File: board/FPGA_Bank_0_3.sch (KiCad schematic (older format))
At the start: 13 parts, among them U10 XC6SLX150T

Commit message: Issue #1680 - Bank 0 Ios
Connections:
- net MAC_SDA: now reaches U10.C1 (IO_L83P_3)
- net MAC_SCL: now reaches U10.G6 (*IO_L82N_3)
- net DIFFIO_B2N: now reaches U10.A17 (IO_L50N_0)
- net DIFFIO_A2N: now reaches U10.A5 (IO_L8N_VREF_0)
- net DIFFIO_B2P: now reaches U10.C17 (IO_L50P_0)
- net DIFFIO_A2P: now reaches U10.C5 (IO_L8P_0)
- net DIFFCLK_B0N: now reaches U10.E16 (IO_L37P_GCLK13_0)
- net DIFFCLK_A1P: now reaches U10.F10 (IO_L34N_GCLK18_0)
- net DIFFCLK_B1N: now reaches U10.F14 (IO_L36P_GCLK15_0)
- net DIFFCLK_B1P: now reaches U10.F15 (IO_L36N_GCLK14_0)
- net DIFFCLK_B0P: now reaches U10.F16 (IO_L37N_GCLK12_0)
- net DIFFIO_B3N: now reaches U10.F17 (IO_L51N_0)
- net DIFFIO_A3N: now reaches U10.F8 (IO_L7N_0)
- net DIFFIO_A1N: now reaches U10.F9 (IO_L32N_0)
- net DIFFCLK_A0P: now reaches U10.G11 (IO_L35N_GCLK16_0)
- net DIFFIO_B0N: now reaches U10.G13 (IO_L38N_VREF_0)
- net DIFFIO_B1N: now reaches U10.G15 (IO_L49N_0)
- net DIFFIO_B3P: now reaches U10.G16 (IO_L51P_0)
- net DIFFIO_A1P: now reaches U10.G8 (IO_L32P_0)
- net DIFFIO_A0P: now reaches U10.H10 (IO_L33P_0)
- net DIFFIO_A0N: now reaches U10.H11 (IO_L33N_0)
- net DIFFCLK_A0N: now reaches U10.H12 (IO_L35P_GCLK17_0)
- net DIFFIO_B0P: now reaches U10.H13 (IO_L38P_0)
- net DIFFIO_B1P: now reaches U10.H14 (IO_L49P_0)
- net RXAUXCH_N renamed DIFFIO_B4N
- net RXAUXCH_P renamed DIFFIO_B4P
- net RXCONFIG1 renamed DIFFIO_B5N
- net RXCONFIG2 renamed DIFFIO_B5P
- net RXHPD renamed DIFFIO_B6P
- net TXAUXCH_N renamed DIFFIO_YP
- net TXAUXCH_P renamed DIFFIO_YN
- net TXCONFIG1 renamed DIFFIO_ZP
- net TXCONFIG2 renamed DIFFIO_ZN
- net TXHPD renamed DIFFIO_B6N
- net USB_D0 renamed DIFFIO_A5P
- net USB_D1 renamed DIFFIO_A6N
- net USB_D2 renamed DIFFIO_A6P
- net USB_D3 renamed DIFFIO_XN
- net USB_D4 renamed DIFFIO_XP
- net USB_D5 renamed DIFFCLK_XN
- net USB_D6 renamed DIFFCLK_XP
- net USB_D7 renamed PCIE_RESET
- net USB_DIR renamed DIFFIO_A4N
- net USB_NXT renamed DIFFIO_A3P
- net USB_REFCLK renamed DIFFCLK_A1N
- net USB_RESETB renamed DIFFIO_A5N
- net USB_STP renamed DIFFIO_A4P
- no-connect marks 7 -> 31

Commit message: Issue #1683
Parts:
- U10: value XC6SLX150T -> XC6SLX45T
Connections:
- net DIFFCLK_A0N: now also U10.F15 (IO_L36N_GCLK14_0); no longer U10.H12 (IO_L35P_GCLK17_0)
- net DIFFCLK_A0P: now also U10.F14 (IO_L36P_GCLK15_0); no longer U10.G11 (IO_L35N_GCLK16_0)
- net DIFFCLK_B1N: now also U10.G11 (IO_L35N_GCLK16_0); no longer U10.F14 (IO_L36P_GCLK15_0)
- net DIFFCLK_B1P: now also U10.H12 (IO_L35P_GCLK17_0); no longer U10.F15 (IO_L36N_GCLK14_0)
- net DIFFCLK_XN: now also U10.D19 (IO_L62N_VREF_0); no longer U10.D5 (IO_L2N_0)
- net DIFFCLK_XP: now also U10.D18 (IO_L62P_0); no longer U10.D4 (IO_L2P_0)
- net DIFFIO_A0N: now also U10.C18 (IO_L66N_SCP0_0); no longer U10.H11 (IO_L33N_0)
- net DIFFIO_A0P: now also U10.D17 (IO_L66P_SCP1_0); no longer U10.H10 (IO_L33P_0)
- net DIFFIO_A1N: now also U10.A18 (IO_L63N_SCP6_0); no longer U10.F9 (IO_L32N_0)
- net DIFFIO_A1P: now also U10.B18 (IO_L63P_SCP7_0); no longer U10.G8 (IO_L32P_0)
- net DIFFIO_A2N: now also U10.G15 (IO_L49N_0); no longer U10.A5 (IO_L8N_VREF_0)
- net DIFFIO_A2P: now also U10.H14 (IO_L49P_0); no longer U10.C5 (IO_L8P_0)
- net DIFFIO_A3N: now also U10.G13 (IO_L38N_VREF_0); no longer U10.F8 (IO_L7N_0)
- net DIFFIO_A3P: now also U10.H13 (IO_L38P_0); no longer U10.F7 (IO_L7P_0)
- net DIFFIO_A4N: now also U10.E6 (IO_L4N_0); no longer U10.A4 (IO_L6N_0)
- net DIFFIO_A4P: now also U10.E5 (IO_L4P_0); no longer U10.C4 (IO_L6P_0)
- net DIFFIO_A5N: now also U10.A4 (IO_L6N_0); no longer U10.A3 (IO_L5N_0)
- net DIFFIO_A5P: now also U10.C4 (IO_L6P_0); no longer U10.B3 (IO_L5P_0)
- net DIFFIO_A6N: now also U10.A2 (IO_L3N_0); no longer U10.E6 (IO_L4N_0)
- net DIFFIO_A6P: now also U10.B2 (IO_L3P_0); no longer U10.E5 (IO_L4P_0)
- net DIFFIO_B0N: now also U10.A20 (IO_L65N_SCP2_0); no longer U10.G13 (IO_L38N_VREF_0)
- net DIFFIO_B0P: now also U10.B20 (IO_L65P_SCP3_0); no longer U10.H13 (IO_L38P_0)
- net DIFFIO_B1N: now also U10.F17 (IO_L51N_0); no longer U10.G15 (IO_L49N_0)
- net DIFFIO_B1P: now also U10.G16 (IO_L51P_0); no longer U10.H14 (IO_L49P_0)
- net DIFFIO_B3N: now also U10.H11 (IO_L33N_0); no longer U10.F17 (IO_L51N_0)
- net DIFFIO_B3P: now also U10.H10 (IO_L33P_0); no longer U10.G16 (IO_L51P_0)
- net DIFFIO_B4N: now also U10.D5 (IO_L2N_0); no longer U10.D19 (IO_L62N_VREF_0)
- net DIFFIO_B4P: now also U10.D4 (IO_L2P_0); no longer U10.D18 (IO_L62P_0)
- net DIFFIO_B5N: now also U10.A5 (IO_L8N_VREF_0); no longer U10.A18 (IO_L63N_SCP6_0)
- net DIFFIO_B5P: now also U10.C5 (IO_L8P_0); no longer U10.B18 (IO_L63P_SCP7_0)
- net DIFFIO_B6N: now also U10.A3 (IO_L5N_0); no longer U10.A19 (IO_L64N_SCP4_0)
- net DIFFIO_B6P: now also U10.B3 (IO_L5P_0); no longer U10.C19 (IO_L64P_SCP5_0)
- net DIFFIO_XN: now also U10.A19 (IO_L64N_SCP4_0); no longer U10.A2 (IO_L3N_0)
- net DIFFIO_XP: now also U10.C19 (IO_L64P_SCP5_0); no longer U10.B2 (IO_L3P_0)
- net DIFFIO_YN: now also U10.F8 (IO_L7N_0); no longer U10.B20 (IO_L65P_SCP3_0)
- net DIFFIO_YP: now also U10.F7 (IO_L7P_0); no longer U10.A20 (IO_L65N_SCP2_0)
- net DIFFIO_ZN: now also U10.F9 (IO_L32N_0); no longer U10.D17 (IO_L66P_SCP1_0)
- net DIFFIO_ZP: now also U10.G8 (IO_L32P_0); no longer U10.C18 (IO_L66N_SCP0_0)
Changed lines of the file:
@@
 $Descr A2 23386 16535
 encoding utf-8
-Sheet 11 12
+Sheet 12 12
 Title "HDMI2USB"
-Date "23 mar 2015"
+Date "25 mar 2015"
 Rev "Rev2"
 Comp ""
@@
 P 3300 6300
 F 0 "U10" H 2350 10350 60  0000 C CNN
-F 1 "XC6SLX150T" H 2650 -1000 60  0000 C CNN
+F 1 "XC6SLX45T" H 2650 -1000 60  0000 C CNN
 F 2 "~" H 3350 6300 60  0000 C CNN
 F 3 "~" H 3350 6300 60  0000 C CNN
@@
 P 19950 9550
 F 0 "U10" H 19000 13600 60  0000 C CNN
-F 1 "XC6SLX150T" H 19300 2250 60  0000 C CNN
+F 1 "XC6SLX45T" H 19300 2250 60  0000 C CNN
 F 2 "~" H 20000 9550 60  0000 C CNN
 F 3 "~" H 20000 9550 60  0000 C CNN
@@
 $EndComp
 $Comp
-L GND #PWR041
+L GND #PWR044
 U 1 1 52E58ED4
 P 12850 14050
-F 0 "#PWR041" H 12850 14050 30  0001 C CNN
+F 0 "#PWR044" H 12850 14050 30  0001 C CNN
 F 1 "GND" H 12850 13980 30  0001 C CNN
 F 2 "" H 12850 14050 60  0000 C CNN
@@
 	4100 1750 3650 1750
 $Comp
-L GND #PWR042
+L GND #PWR045
 U 1 1 52EB777D
 P 3650 1900
-F 0 "#PWR042" H 3650 1900 30  0001 C CNN
+F 0 "#PWR045" H 3650 1900 30  0001 C CNN
 F 1 "GND" H 3650 1830 30  0001 C CNN
 F 2 "" H 3650 1900 60  0000 C CNN
@@
 Connection ~ 9650 13150
 $Comp
-L GND #PWR043
+L GND #PWR046
 U 1 1 5387725D
 P 9850 13950
-F 0 "#PWR043" H 9850 13950 30  0001 C CNN
+F 0 "#PWR046" H 9850 13950 30  0001 C CNN
 F 1 "GND" H 9850 13880 30  0001 C CNN
 F 2 "" H 9850 13950 60  0000 C CNN
@@
 Text Notes 20050 2000 0    157  ~ 31
 BANK 0
-Text HLabel 19200 10150 0    39   BiDi ~ 0
+Text HLabel 19200 8750 0    39   BiDi ~ 0
 DIFFIO_B0P
-Text HLabel 19200 9950 0    39   BiDi ~ 0
+Text HLabel 19200 9550 0    39   BiDi ~ 0
 DIFFIO_B1P
 Text HLabel 19200 9750 0    39   BiDi ~ 0
 DIFFIO_B2P
-Text HLabel 19200 9550 0    39   BiDi ~ 0
+Text HLabel 19200 11150 0    39   BiDi ~ 0
 DIFFIO_B3P
-Text HLabel 19200 9350 0    39   BiDi ~ 0
+Text HLabel 19200 12750 0    39   BiDi ~ 0
 DIFFIO_B4P
-Text HLabel 19200 9150 0    39   BiDi ~ 0
+Text HLabel 19200 11550 0    39   BiDi ~ 0
 DIFFIO_B5P
-Text HLabel 19200 8950 0    39   BiDi ~ 0
+Text HLabel 19200 12150 0    39   BiDi ~ 0
 DIFFIO_B6P
-Text HLabel 19200 10050 0    39   BiDi ~ 0
+Text HLabel 19200 8650 0    39   BiDi ~ 0
 DIFFIO_B0N
-Text HLabel 19200 9850 0    39   BiDi ~ 0
+Text HLabel 19200 9450 0    39   BiDi ~ 0
 DIFFIO_B1N
 Text HLabel 19200 9650 0    39   BiDi ~ 0
 DIFFIO_B2N
-Text HLabel 19200 9450 0    39   BiDi ~ 0
+Text HLabel 19200 11050 0    39   BiDi ~ 0
 DIFFIO_B3N
-Text HLabel 19200 9250 0    39   BiDi ~ 0
+Text HLabel 19200 12650 0    39   BiDi ~ 0
 DIFFIO_B4N
+Text HLabel 19200 11450 0    39   BiDi ~ 0
+DIFFIO_B5N
+Text HLabel 19200 12050 0    39   BiDi ~ 0
+DIFFIO_B6N
+Text HLabel 19200 8450 0    39   BiDi ~ 0
+DIFFIO_A0N
 Text HLabel 19200 9050 0    39   BiDi ~ 0
-DIFFIO_B5N
-Text HLabel 19200 8850 0    39   BiDi ~ 0
-DIFFIO_B6N
-Text HLabel 19200 11050 0    39   BiDi ~ 0
-DIFFIO_A0N
-Text HLabel 19200 11250 0    39   BiDi ~ 0
 DIFFIO_A1N
-Text HLabel 19200 11450 0    39   BiDi ~ 0
+Text HLabel 19200 9850 0    39   BiDi ~ 0
 DIFFIO_A2N
-Text HLabel 19200 11650 0    39   BiDi ~ 0
+Text HLabel 19200 10050 0    39   BiDi ~ 0
 DIFFIO_A3N
+Text HLabel 19200 12250 0    39   BiDi ~ 0
+DIFFIO_A4N
 Text HLabel 19200 11850 0    39   BiDi ~ 0
-DIFFIO_A4N
-Text HLabel 19200 12050 0    39   BiDi ~ 0
 DIFFIO_A5N
-Text HLabel 19200 12250 0    39   BiDi ~ 0
+Text HLabel 19200 12450 0    39   BiDi ~ 0
 DIFFIO_A6N
-Text HLabel 19200 11150 0    39   BiDi ~ 0
+Text HLabel 19200 8550 0    39   BiDi ~ 0
 DIFFIO_A0P
-Text HLabel 19200 11350 0    39   BiDi ~ 0
+Text HLabel 19200 9150 0    39   BiDi ~ 0
 DIFFIO_A1P
-Text HLabel 19200 11550 0    39   BiDi ~ 0
+Text HLabel 19200 9950 0    39   BiDi ~ 0
 DIFFIO_A2P
-Text HLabel 19200 11750 0    39   BiDi ~ 0
+Text HLabel 19200 10150 0    39   BiDi ~ 0
 DIFFIO_A3P
+Text HLabel 19200 12350 0    39   BiDi ~ 0
+DIFFIO_A4P
 Text HLabel 19200 11950 0    39   BiDi ~ 0
-DIFFIO_A4P
-Text HLabel 19200 12150 0    39   BiDi ~ 0
 DIFFIO_A5P
-Text HLabel 19200 12350 0    39   BiDi ~ 0
+Text HLabel 19200 12550 0    39   BiDi ~ 0
 DIFFIO_A6P
 Text HLabel 19200 10250 0    39   BiDi ~ 0
 DIFFCLK_B0P
-Text HLabel 19200 10450 0    39   BiDi ~ 0
+Text HLabel 19200 10750 0    39   BiDi ~ 0
 DIFFCLK_B1P
 Text HLabel 19200 10350 0    39   BiDi ~ 0
 DIFFCLK_B0N
-Text HLabel 19200 10550 0    39   BiDi ~ 0
+Text HLabel 19200 10650 0    39   BiDi ~ 0
 DIFFCLK_B1N
-Text HLabel 19200 10750 0    39   BiDi ~ 0
+Text HLabel 19200 10450 0    39   BiDi ~ 0
 DIFFCLK_A0N
 Text HLabel 19200 10950 0    39   BiDi ~ 0
 DIFFCLK_A1N
-Text HLabel 19200 10650 0    39   BiDi ~ 0
+Text HLabel 19200 10550 0    39   BiDi ~ 0
 DIFFCLK_A0P
 Text HLabel 19200 10850 0    39   BiDi ~ 0
 DIFFCLK_A1P
-Text HLabel 19200 8550 0    39   BiDi ~ 0
+Text HLabel 19200 11250 0    39   BiDi ~ 0
 DIFFIO_ZN
-Text HLabel 19200 8450 0    39   BiDi ~ 0
+Text HLabel 19200 11350 0    39   BiDi ~ 0
 DIFFIO_ZP
-Text HLabel 19200 12450 0    39   BiDi ~ 0
+Text HLabel 19200 8850 0    39   BiDi ~ 0
 DIFFIO_XN
-Text HLabel 19200 12550 0    39   BiDi ~ 0
+Text HLabel 19200 8950 0    39   BiDi ~ 0
 DIFFIO_XP
-Text HLabel 19200 8750 0    39   BiDi ~ 0
+Text HLabel 19200 11650 0    39   BiDi ~ 0
 DIFFIO_YN
-Text HLabel 19200 8650 0    39   BiDi ~ 0
+Text HLabel 19200 11750 0    39   BiDi ~ 0
 DIFFIO_YP
 Text HLabel 19200 12850 0    39   Input ~ 0
 PCIE_RESET
-Text HLabel 19200 12750 0    39   BiDi ~ 0
+Text HLabel 19200 9350 0    39   BiDi ~ 0
 DIFFCLK_XP
-Text HLabel 19200 12650 0    39   BiDi ~ 0
+Text HLabel 19200 9250 0    39   BiDi ~ 0
 DIFFCLK_XN
 Wire Wire Line

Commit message: Issue #1670
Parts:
- added R68: 50R, ~, symbol R
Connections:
- net GTP1V2: now also R68.1; no longer U10.E9 (MGTRREF_101)
- net RX_LANEN0 renamed DPRX_LANEN0
- net RX_LANEN1 renamed DPRX_LANEN1
- net RX_LANEN2 renamed DPRX_LANEN2
- net RX_LANEN3 renamed DPRX_LANEN3
- net RX_LANEP0 renamed DPRX_LANEP0
- net RX_LANEP1 renamed DPRX_LANEP1
- net RX_LANEP2 renamed DPRX_LANEP2
- net RX_LANEP3 renamed DPRX_LANEP3
- net TX_LANEN0 renamed DPTX_LANEN0
- net TX_LANEN1 renamed DPTX_LANEN1
- net TX_LANEN2 renamed DPTX_LANEN2
- net TX_LANEN3 renamed DPTX_LANEN3
- net TX_LANEP0 renamed DPTX_LANEP0
- net TX_LANEP1 renamed DPTX_LANEP1
- net TX_LANEP2 renamed DPTX_LANEP2
- net TX_LANEP3 renamed DPTX_LANEP3
- new net: R68.2, U10.E9 (MGTRREF_101)

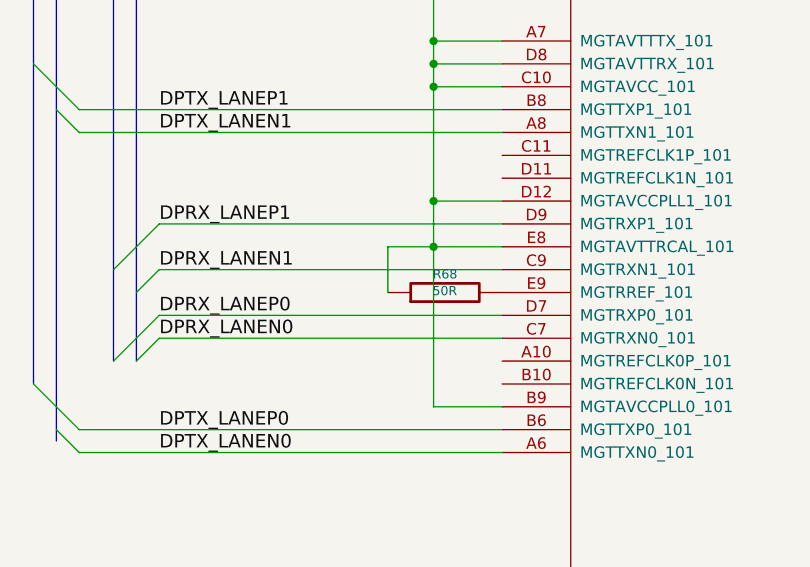
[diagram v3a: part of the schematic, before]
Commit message: Issue #1488 - Added diode display port power pin
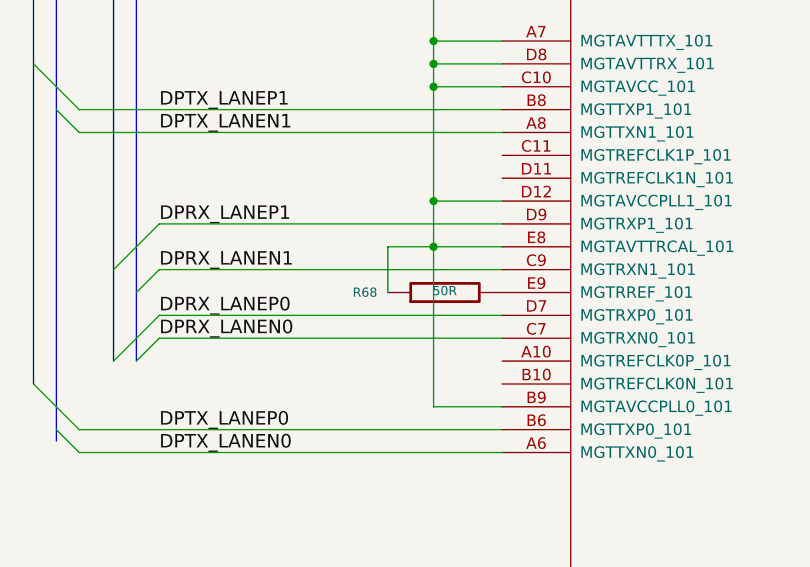
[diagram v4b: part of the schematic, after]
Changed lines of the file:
@@
 $EndComp
 $Comp
-L GND #PWR044
+L GND #PWR46
 U 1 1 52E58ED4
 P 12850 14050
-F 0 "#PWR044" H 12850 14050 30  0001 C CNN
+F 0 "#PWR46" H 12850 14050 30  0001 C CNN
 F 1 "GND" H 12850 13980 30  0001 C CNN
 F 2 "" H 12850 14050 60  0000 C CNN
@@
 $EndComp
 $Comp
-L GND #PWR045
+L GND #PWR44
 U 1 1 52EB777D
 P 3650 1900
-F 0 "#PWR045" H 3650 1900 30  0001 C CNN
+F 0 "#PWR44" H 3650 1900 30  0001 C CNN
 F 1 "GND" H 3650 1830 30  0001 C CNN
 F 2 "" H 3650 1900 60  0000 C CNN
@@
 $EndComp
 $Comp
-L GND #PWR046
+L GND #PWR45
 U 1 1 5387725D
 P 9850 13950
-F 0 "#PWR046" H 9850 13950 30  0001 C CNN
+F 0 "#PWR45" H 9850 13950 30  0001 C CNN
 F 1 "GND" H 9850 13880 30  0001 C CNN
 F 2 "" H 9850 13950 60  0000 C CNN
@@
 U 1 1 551D0351
 P 18950 7150
-F 0 "R68" V 19030 7150 40  0000 C CNN
+F 0 "R68" V 18950 7500 40  0000 C CNN
 F 1 "50R" V 18957 7151 40  0000 C CNN
 F 2 "~" V 18880 7150 30  0000 C CNN

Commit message: Issue #1585
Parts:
- added C245, C246, C247, C248, C249, C250: 0.1UF, symbol C
- added R120: 4.7K, ~, symbol R
- added U27: FXO-LC73, ~, symbol FXO-LC73
- added U28, U29: SMA_CON, ~, symbol SMA_CON
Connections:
- net GND: now also U27.3 (GND), U28.1, U29.1
- net PCIO3: now reaches U10.F5 (*IO_L82P_3)
- net PCIO0: now reaches U10.G7 (*IO_L80N_3)
- net PCIO2: now reaches U10.H8 (*IO_L81N_3)
- net PCIO1: now reaches U10.J7 (*IO_L81P_3)
- net at U10.A10 (MGTREFCLK0P_101): now also C245.2
- net at U10.B10 (MGTREFCLK0N_101): now also C246.2
- net MGTSMACLK_P: now reaches U10.C11 (MGTREFCLK1P_101)
- net MGTSMACLK_P: now also C249.1
- net MGTSMACLK_N: now reaches U10.D11 (MGTREFCLK1N_101)
- net MGTSMACLK_N: now also C250.1
- net MGT127MHz_P: now reaches U10.E12 (*MGTREFCLK1P_123)
- net MGT127MHz_P: now also C248.1
- net MGT127MHz_N: now reaches U10.F12 (*MGTREFCLK1N_123)
- net MGT127MHz_N: now also C247.1
- new net: C248.2, U27.4 (OUT)
- new net: C247.2, U27.5 (OUT_2#)
- new net: C250.2, U28.2
- new net: C249.2, U29.2
- new net: R120.1, U27.1 (E/D)
- new net MGTREFCLK0_101_N: C246.1
- new net MGTREFCLK0_101_P: C245.1
- new net VCC3V3: R120.2, U27.6 (VCC)
- no-connect marks 31 -> 29

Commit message: Issue #1647 - Final changes
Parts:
- added P15: CONN_5, symbol CONN_5
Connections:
- net GND: now also P15.5
- net GTP1V2: no longer R68.1, U10.A15 (MGTAVTTTX_123), U10.A7 (MGTAVTTTX_101), U10.B13 (*MGTAVCCPLL0_123), U10.B9 (MGTAVCCPLL0_101), U10.C10 (MGTAVCC_101), U10.D12 (MGTAVCCPLL1_101), U10.D14 (MGTAVTTRX_123), U10.D8 (MGTAVTTRX_101), U10.E10 (MGTAVCC_123), U10.E13 (*MGTAVCCPLL1_123), U10.E8 (MGTAVTTRCAL_101)
- net VCC3V3: now also P15.1
- net DEBUG_IO0: now reaches U10.E4 (IO_L60N_3)
- net DEBUG_IO0: now also P15.3
- net DEBUG_IO1: now reaches U10.H6 (*IO_L80P_3)
- net DEBUG_IO1: now also P15.4
- net MGT127MHz_N renamed MGT135MHz_N
- net MGT127MHz_P renamed MGT135MHz_P
- new net VCC1V2: P15.2, R68.1, U10.A15 (MGTAVTTTX_123), U10.A7 (MGTAVTTTX_101), U10.B13 (*MGTAVCCPLL0_123), U10.B9 (MGTAVCCPLL0_101), U10.C10 (MGTAVCC_101), U10.D12 (MGTAVCCPLL1_101), U10.D14 (MGTAVTTRX_123), U10.D8 (MGTAVTTRX_101), U10.E10 (MGTAVCC_123), U10.E13 (*MGTAVCCPLL1_123), U10.E8 (MGTAVTTRCAL_101)
- no-connect marks 29 -> 27

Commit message: Issue #1713
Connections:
- net GTP1V2 is gone; now on net VCC1V2: C191.1, C193.1, C194.1, C195.1, C196.1, C197.1, C198.1, C199.1, C200.1
- net DEBUG_IO0: now also U10.AA2 (IO_L10P_3); no longer U10.E4 (IO_L60N_3)
- net DEBUG_IO1: now also U10.AA1 (IO_L10N_3); no longer U10.H6 (*IO_L80P_3)
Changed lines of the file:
@@
 Sheet 11 12
 Title "HDMI2USB"
-Date "2 apr 2015"
+Date "7 apr 2015"
 Rev "Rev2"
 Comp ""
@@
 $EndComp
 $Comp
-L GND #PWR047
+L GND #PWR048
 U 1 1 52E58ED4
 P 12850 14050
-F 0 "#PWR047" H 12850 14050 30  0001 C CNN
+F 0 "#PWR048" H 12850 14050 30  0001 C CNN
 F 1 "GND" H 12850 13980 30  0001 C CNN
 F 2 "" H 12850 14050 60  0000 C CNN
@@
 	1    0    0    -1
 $EndComp
-Text Label 14350 13150 2    60   ~ 0
-GTP1V2
 NoConn ~ 4050 4650
 $Comp
@@
 $EndComp
 $Comp
-L GND #PWR048
+L GND #PWR049
 U 1 1 52EB777D
 P 3650 1900
-F 0 "#PWR048" H 3650 1900 30  0001 C CNN
+F 0 "#PWR049" H 3650 1900 30  0001 C CNN
 F 1 "GND" H 3650 1830 30  0001 C CNN
 F 2 "" H 3650 1900 60  0000 C CNN
@@
 $EndComp
 $Comp
-L GND #PWR049
+L GND #PWR050
 U 1 1 5387725D
 P 9850 13950
-F 0 "#PWR049" H 9850 13950 30  0001 C CNN
+F 0 "#PWR050" H 9850 13950 30  0001 C CNN
 F 1 "GND" H 9850 13880 30  0001 C CNN
 F 2 "" H 9850 13950 60  0000 C CNN
@@
 NoConn ~ 4050 3950
 NoConn ~ 4050 3850
-NoConn ~ 4050 3750
-NoConn ~ 4050 3650
 NoConn ~ 4050 3550
 NoConn ~ 4050 3450
@@
 $EndComp
 $Comp
-L GND #PWR050
+L GND #PWR051
 U 1 1 55233CE0
 P 16200 13150
-F 0 "#PWR050" H 16200 13150 30  0001 C CNN
+F 0 "#PWR051" H 16200 13150 30  0001 C CNN
 F 1 "GND" H 16200 13080 30  0001 C CNN
 F 2 "" H 16200 13150 60  0000 C CNN
@@
 $EndComp
 $Comp
-L GND #PWR051
+L GND #PWR052
 U 1 1 55236BCD
 P 14150 15200
-F 0 "#PWR051" H 14150 15200 30  0001 C CNN
+F 0 "#PWR052" H 14150 15200 30  0001 C CNN
 F 1 "GND" H 14150 15130 30  0001 C CNN
 F 2 "" H 14150 15200 60  0000 C CNN
@@
 	1    0    0    -1
 $EndComp
-Text Label 4550 10350 2    39   ~ 0
+Text Label 4550 3650 2    39   ~ 0
 DEBUG_IO0
-Text Label 4550 10450 2    39   ~ 0
+Text Label 4550 3750 2    39   ~ 0
 DEBUG_IO1
 Text Label 7450 13950 0    39   ~ 0
@@
 VCC1V2
 $Comp
-L GND #PWR052
+L GND #PWR053
 U 1 1 551D8F91
 P 7950 14250
-F 0 "#PWR052" H 7950 14250 30  0001 C CNN
+F 0 "#PWR053" H 7950 14250 30  0001 C CNN
 F 1 "GND" H 7950 14180 30  0001 C CNN
 F 2 "" H 7950 14250 60  0000 C CNN
@@
 	18000 6650 19200 6650
 Wire Wire Line
-	4050 10450 4550 10450
-Wire Wire Line
-	4050 10350 4550 10350
+	4050 3750 4550 3750
+Wire Wire Line
+	4050 3650 4550 3650
 Wire Wire Line
 	7950 14050 7450 14050
@@
 Wire Wire Line
 	7950 14150 7950 14250
+NoConn ~ 4050 10450
+NoConn ~ 4050 10350
+Text Label 14350 13150 2    39   ~ 0
+VCC1V2
 $EndSCHEMATC

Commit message: Issue #1713
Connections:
- net VCC1V2: no longer P15.2
- new net VCC1V5: P15.2
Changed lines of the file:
@@
 Sheet 11 12
 Title "HDMI2USB"
-Date "7 apr 2015"
+Date "8 apr 2015"
 Rev "Rev2"
 Comp ""
@@
 Text Label 18500 3550 0    39   ~ 0
 VCC1V2
-Text Label 7450 13850 0    39   ~ 0
-VCC1V2
 $Comp
 L GND #PWR053
@@
 Text Label 14350 13150 2    39   ~ 0
 VCC1V2
+Text Label 7450 13850 0    39   ~ 0
+VCC1V5
+Text GLabel 7450 13850 0    39   Input ~ 0
+VCC1V5
 $EndSCHEMATC
